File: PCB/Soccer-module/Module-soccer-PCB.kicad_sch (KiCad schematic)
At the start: 6 parts, among them J2 Conn_01x06, J4 Conn_01x02, J5 Conn_01x02, J6 Conn_01x02, U1 TB6612

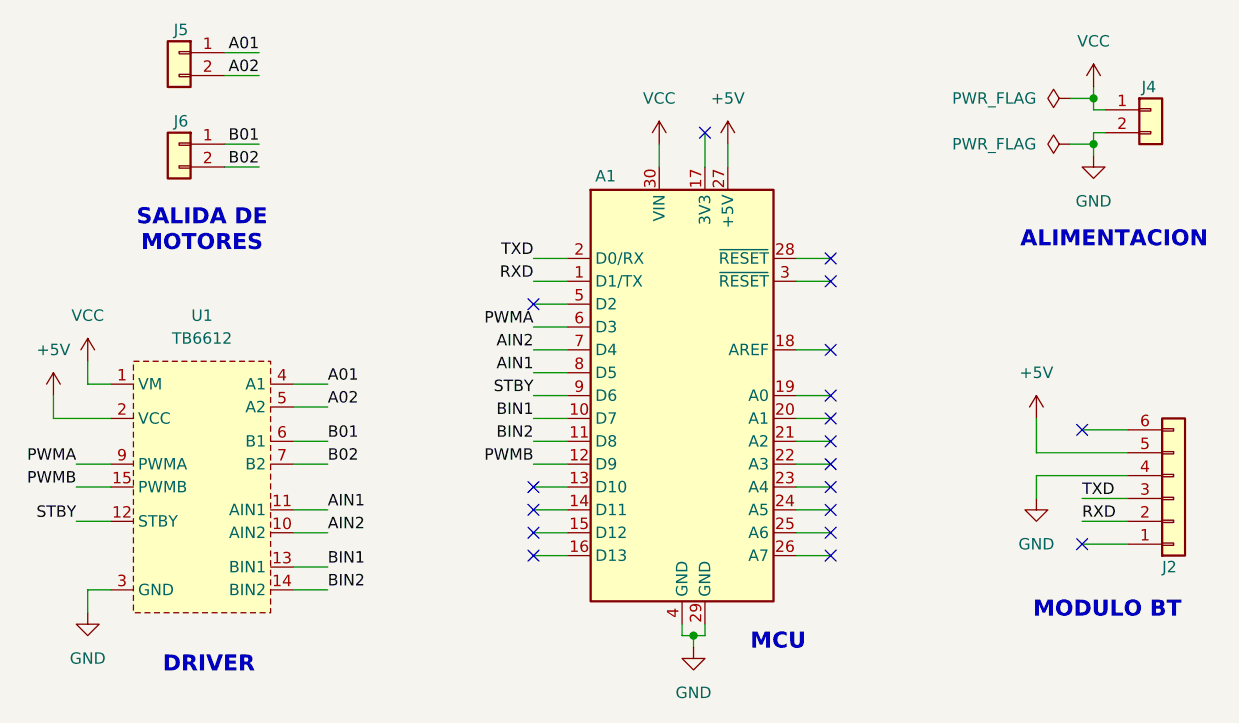
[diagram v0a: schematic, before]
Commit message: Nuevos modelos del esquematico
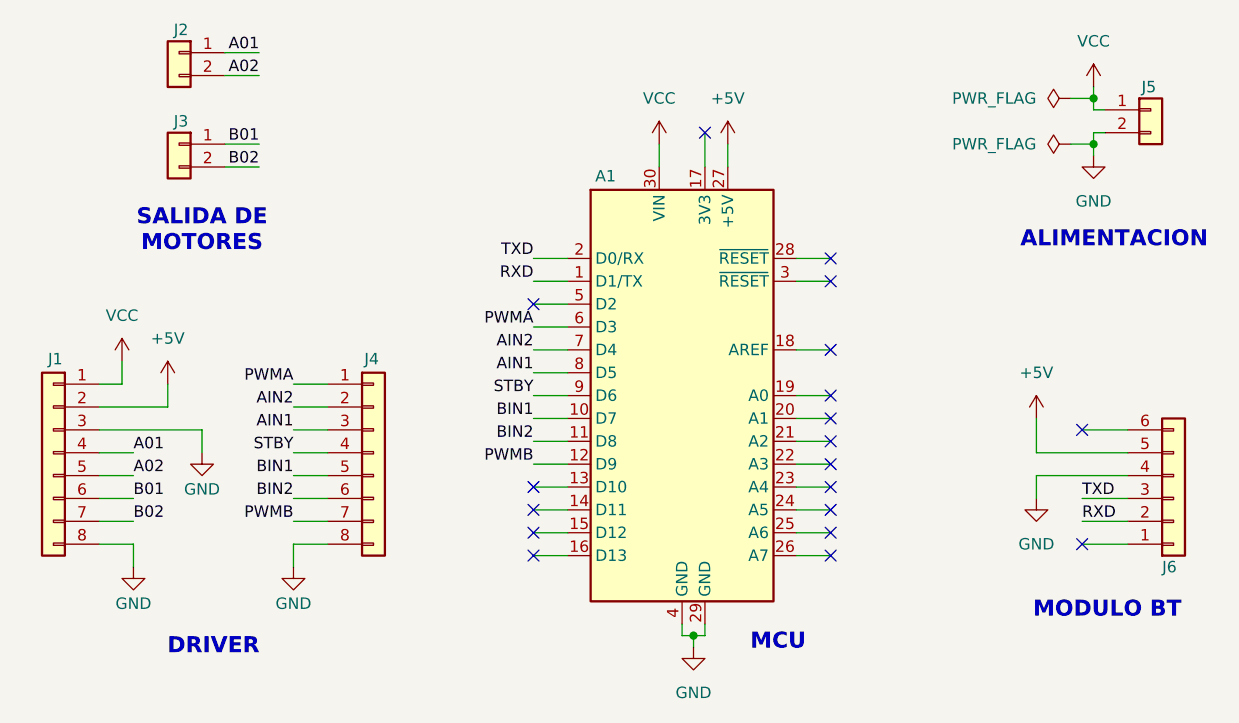
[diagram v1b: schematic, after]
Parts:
- removed U1: TB6612, Footprints-soccer:TB6612_17.8x15, symbol Soccer-symbols:TB6612
- added J1, J4: Conn_01x08, Connector_PinSocket_2.54mm:PinSocket_1x08_P2.54mm_Vertical, symbol Connector_Generic:Conn_01x08
- renumbered J5 to J2, J6 to J3, J4 to J5, J2 to J6
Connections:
- net +5V: now also J1.2 (Pin_2)
- net A01: now also J1.4 (Pin_4)
- net A02: now also J1.5 (Pin_5)
- net AIN1: now also J4.3 (Pin_3)
- net AIN2: now also J4.2 (Pin_2)
- net B01: now also J1.6 (Pin_6)
- net B02: now also J1.7 (Pin_7)
- net BIN1: now also J4.5 (Pin_5)
- net BIN2: now also J4.6 (Pin_6)
- net GND: now also J1.3 (Pin_3), J1.8 (Pin_8), J4.8 (Pin_8)
- net PWMA: now also J4.1 (Pin_1)
- net PWMB: now also J4.7 (Pin_7)
- net STBY: now also J4.4 (Pin_4)
- net VCC: now also J1.1 (Pin_1)
